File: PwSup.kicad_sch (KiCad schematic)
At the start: 16 parts

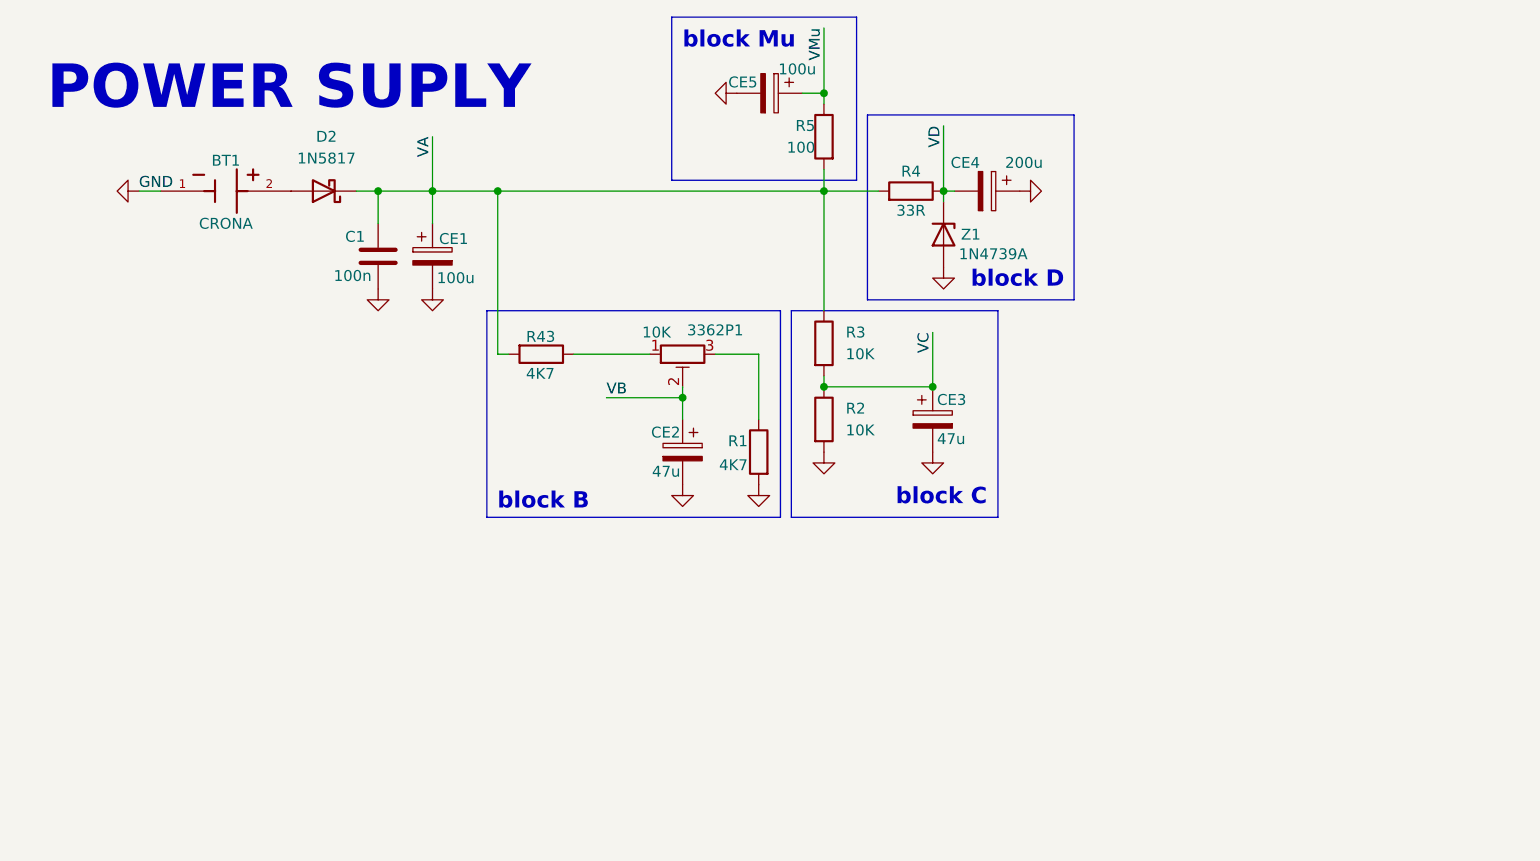
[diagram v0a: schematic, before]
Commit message: power supply upd
9v pover supply changed on AC-DC tancformer
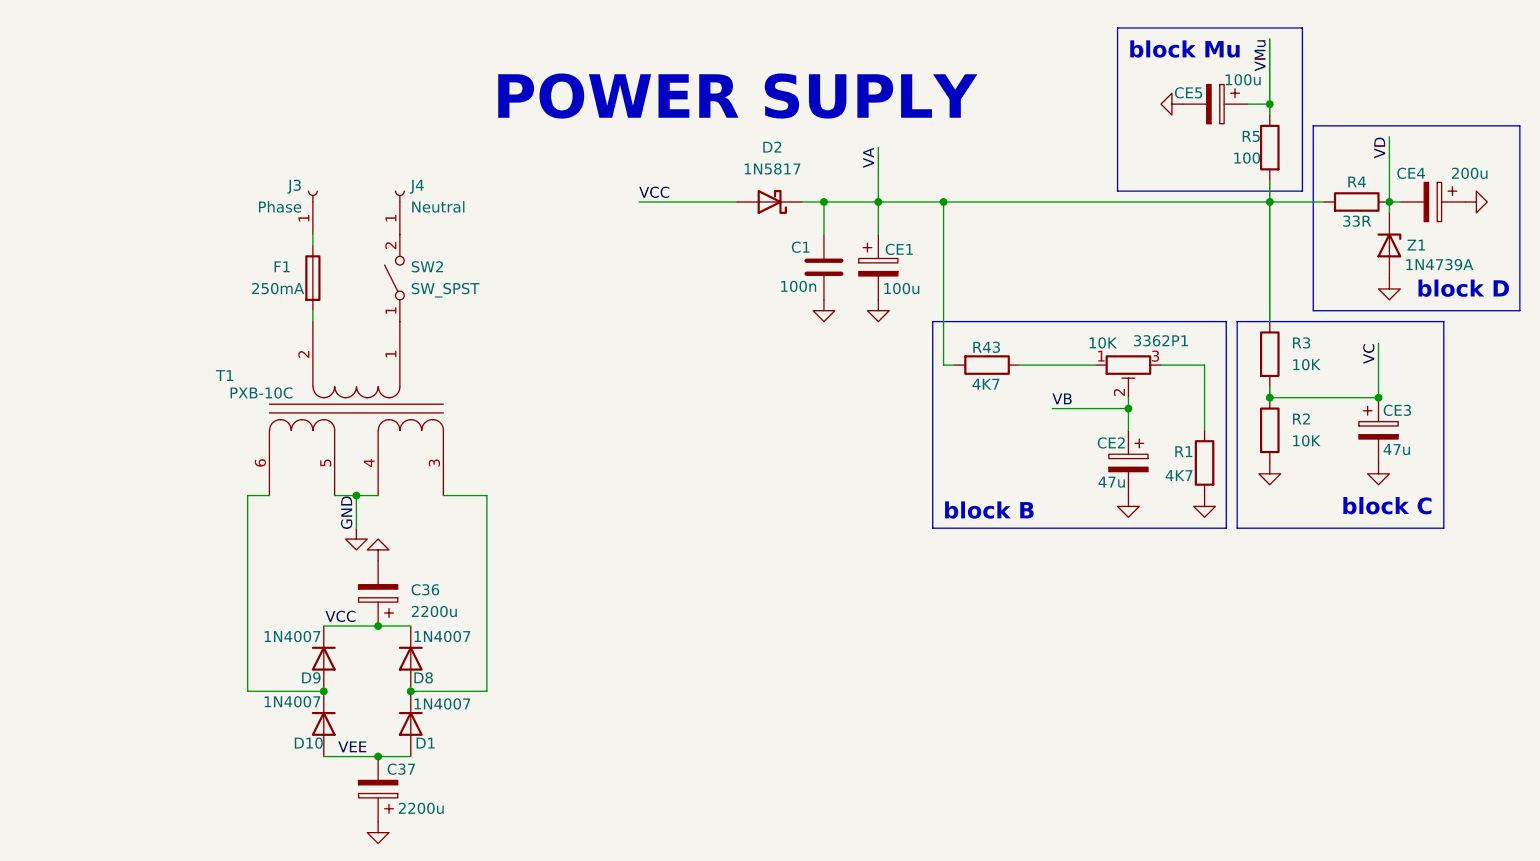
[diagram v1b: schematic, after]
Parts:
- removed BT1: CRONA, Connector_PinHeader_2.54mm:PinHeader_1x02_P2.54mm_Vertical, symbol IMP_LIB_SYM:BH23APC
- added C36, C37: 2200u, symbol Device:C_Polarized
- added D1, D10, D8, D9: 1N4007, Diode_THT:D_DO-41_SOD81_P10.16mm_Horizontal, symbol Diode:1N4007
- added F1: 250mA, symbol Device:Fuse
- added J3: Phase, Connector_Phoenix_SPT:PhoenixContact_SPT_2.5_1-H-5.0_1x01_P5.0mm_Horizontal, symbol Connector:Conn_01x01_Socket
- added J4: Neutral, symbol Connector:Conn_01x01_Socket
- added SW2: SW_SPST, symbol Switch:SW_SPST
- added T1: PXB-10C, symbol Device:Transformer_1P_2S
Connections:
- net GND: now also C36.2, C37.1, T1.4 (SB), T1.5 (SC)
- net VCC: now reaches D2.2 (A)
- net VCC: now also C36.1, D8.1 (K), D9.1 (K)
- new net: J4.1 (Pin_1), SW2.2 (B)
- new net: D1.1 (K), D8.2 (A), T1.3 (SA)
- new net: D10.1 (K), D9.2 (A), T1.6 (SD)
- new net: F1.1, J3.1 (Pin_1)
- new net: F1.2, T1.2 (AB)
- new net: SW2.1 (A), T1.1 (AA)
- new net VEE: C37.2, D1.2 (A), D10.2 (A)
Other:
- moved on the sheet: 3362P1, C1, CE1, CE2, CE3, CE4, CE5, D2, R1, R2, R3, R4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
